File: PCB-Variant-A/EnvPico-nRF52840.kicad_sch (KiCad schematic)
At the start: 49 parts, among them J3 2.54mm header 01x20, J4 2.54mm header 01x20, J5 Conn_01x03_Male, U1 LM3671MF 3.3, U101 nRF52840_holyiot_18010, U2 BQ24072RGT, U3 nRF52840, Y1 32MHz 12pF

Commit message: made a couple of pcb variants for future use maybe
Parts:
- removed U101: nRF52840_holyiot_18010, EnvExtras:nRF52840_holyiot_18010, symbol nrf52840_holyiot_18010:nRF52840_holyiot_18010-kicad-keyboard-parts-ahokore-resc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
- added U4: holyiot-18010, mcu:holyiot-18010, symbol mcu:holyiot-18010
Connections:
- net GND: now also U4.1 (GND), U4.32 (GND), U4.44 (GND)
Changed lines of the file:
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@@
     (pin "2")
   )
-  (symbol (lib_id "nrf52840_holyiot_18010:nRF52840_holyiot_18010-kicad-keyboard-parts-ahokore-rescue") (at 52.07 172.085 0) (unit 1)
+  (symbol (lib_id "mcu:holyiot-18010") (at 44.958 174.752 0) (unit 1)
     (in_bom yes) (on_board yes) (fields_autoplaced)
-    (property "Reference" "U101" (id 0) (at 52.07 132.08 0))
-    (property "Value" "nRF52840_holyiot_18010" (id 1) (at 52.07 134.62 0))
-    (property "Footprint" "EnvExtras:nRF52840_holyiot_18010" (id 2) (at 54.61 161.925 0)
-      (effects (font (size 1.27 1.27)) hide)
-    )
-    (property "Datasheet" "http://www.holyiot.com/tp/2019042516322180424.pdf" (id 3) (at 54.61 161.925 0)
+    (property "Reference" "U4" (id 0) (at 44.958 130.302 0))
+    (property "Value" "holyiot-18010" (id 1) (at 44.958 132.842 0))
+    (property "Footprint" "mcu:holyiot-18010" (id 2) (at 44.958 127.762 0)
+      (effects (font (size 1.27 1.27)) hide)
+    )
+    (property "Datasheet" "" (id 3) (at 83.058 200.152 0)
       (effects (font (size 1.27 1.27)) hide)
     )
@@
     (pin "41")
     (pin "42")
-    (pin "42")
     (pin "43")
+    (pin "44")
     (pin "45")
     (pin "46")
@@
       (reference "U3") (unit 1) (value "nRF52840") (footprint "Package_DFN_QFN:Nordic_AQFN-73-1EP_7x7mm_P0.5mm")
     )
-    (path "/8ee0b195-44f0-4b21-9341-8dba1a90f90e"
-      (reference "U101") (unit 1) (value "nRF52840_holyiot_18010") (footprint "EnvExtras:nRF52840_holyiot_18010")
+    (path "/a4716bf7-5af8-4864-9cee-c215b7ab03ab"
+      (reference "U4") (unit 1) (value "holyiot-18010") (footprint "mcu:holyiot-18010")
     )
     (path "/00000000-0000-0000-0000-00005edb7d8d"

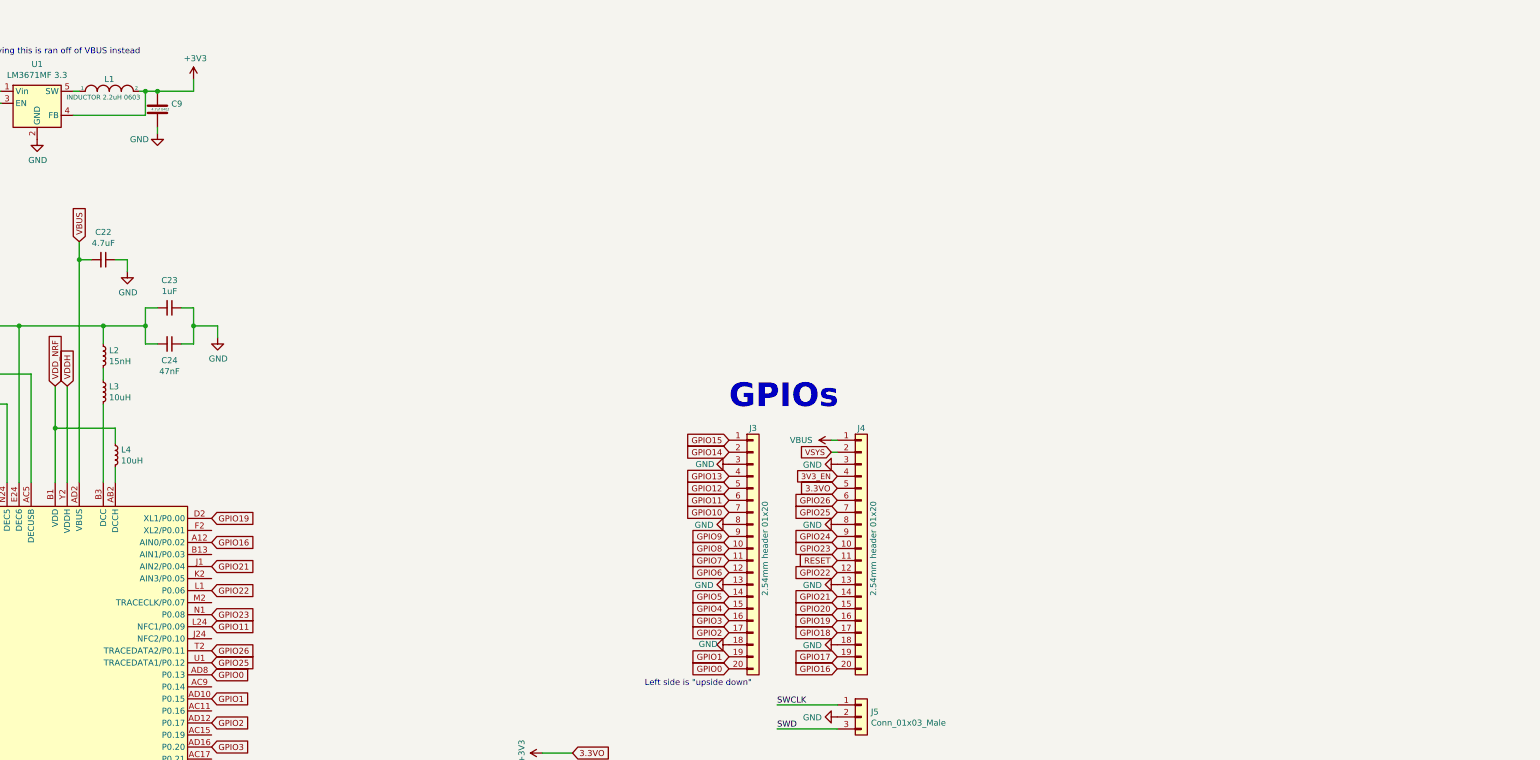
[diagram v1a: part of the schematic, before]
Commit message: added library for QFN version
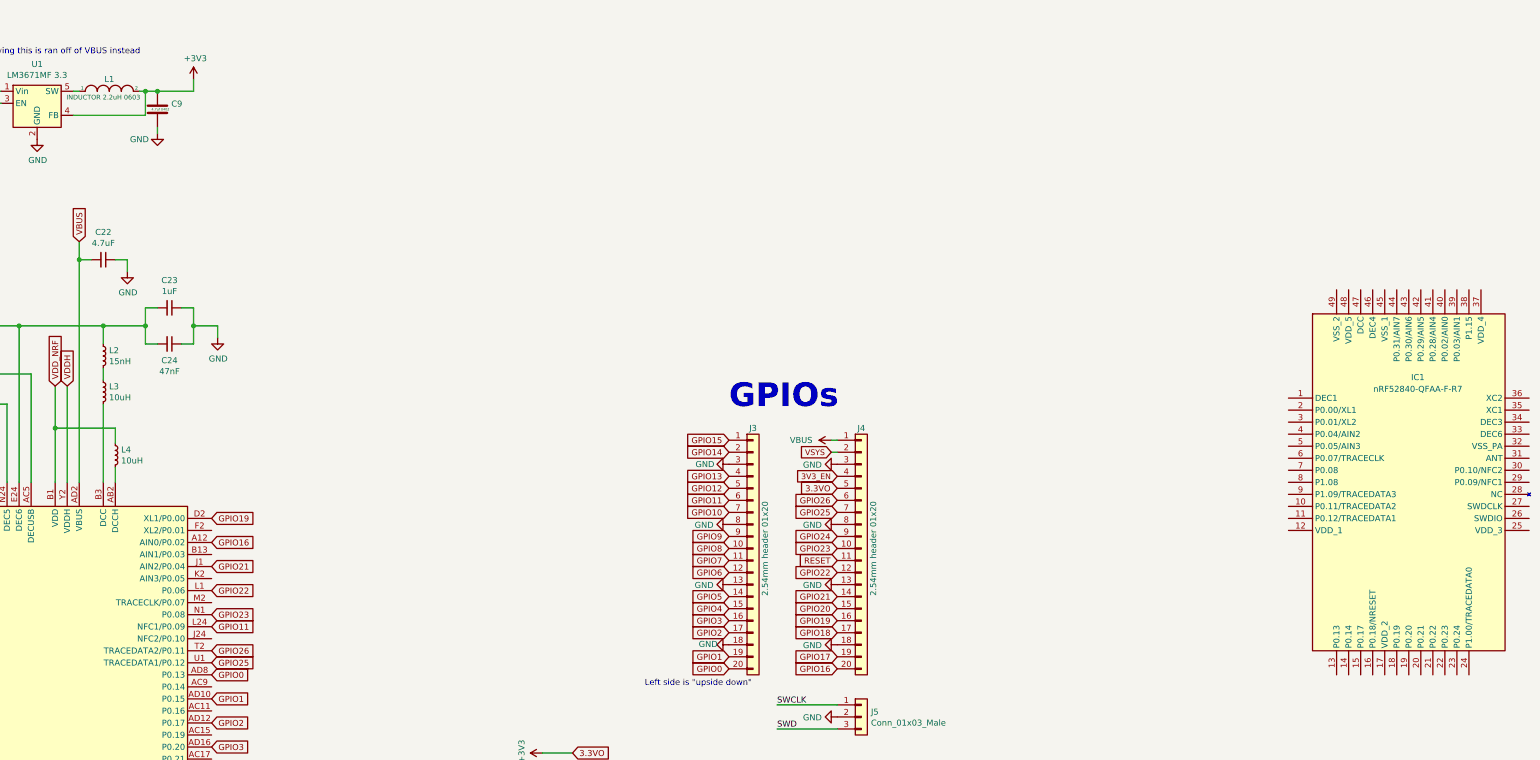
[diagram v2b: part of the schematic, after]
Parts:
- added IC1: nRF52840-QFAA-F-R7, QFN40P600X600X95-49N-D, symbol nRF52840-QFAA-F-R7:nRF52840-QFAA-F-R7

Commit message: started re-design of board.
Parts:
- removed C13: 0402 1pF, Capacitor_SMD:C_0402_1005Metric, symbol Device:C_Small
- removed C8: 0402 1.5pF, Capacitor_SMD:C_0402_1005Metric, symbol Device:C_Small
- removed IC1: nRF52840-QFAA-F-R7, QFN40P600X600X95-49N-D, symbol nRF52840-QFAA-F-R7:nRF52840-QFAA-F-R7
- removed NT1: Net-Tie_2, NetTie:NetTie-2_SMD_Pad0.5mm, symbol Device:Net-Tie_2
- removed R1: 0R 0402, Resistor_SMD:R_0402_1005Metric, symbol Device:R_Small
- removed U4: holyiot-18010, mcu:holyiot-18010, symbol mcu:holyiot-18010
- added L5: 5.6nH 0402, Inductor_SMD:L_0402_1005Metric, symbol Device:L_Small
- AE1: footprint RF_Antenna:Texas_SWRA117D_2.4GHz_Left -> RF_Antenna:Johanson_2450AT43F0100
- C14: value 0402 1pF -> 0402 0.8pF
- C15: value 100nF -> 100nF 0402
- C16: value 100pF -> 100pF 0402
- C17: value 1nF -> 820pF 0402 - DNP
- J5: value Conn_01x03_Male -> BM03B 3P; footprint Connector_PinHeader_2.54mm:PinHeader_1x03_P2.54mm_Vertical -> Connector_JST:JST_SUR_BM03B-SURS-TF_1x03-1MP_P0.80mm_Vertical
- Y1: value 32MHz 12pF -> 32MHz 12pF 2016-4P; footprint Crystal:Crystal_SMD_3225-4Pin_3.2x2.5mm -> Crystal:Crystal_SMD_2016-4Pin_2.0x1.6mm
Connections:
- net VSS_PA is gone; now on net GND: C14.2, U3.F23 (VSS_PA)
- net +3V3: no longer J4.5 (Pin_5)
- net 3V3_EN: no longer J4.4 (Pin_4)
- net GND: no longer J3.13 (Pin_13), J3.18 (Pin_18), J3.3 (Pin_3), J3.8 (Pin_8), J4.13 (Pin_13), J4.18 (Pin_18), J4.3 (Pin_3), J4.8 (Pin_8)
- net GPIO0: no longer J3.20 (Pin_20)
- net GPIO1: no longer J3.19 (Pin_19)
- net GPIO10: no longer J3.7 (Pin_7)
- net GPIO11: no longer J3.6 (Pin_6)
- net GPIO12: no longer J3.5 (Pin_5)
- net GPIO13: no longer J3.4 (Pin_4)
- net GPIO14: no longer J3.2 (Pin_2)
- net GPIO15: no longer J3.1 (Pin_1)
- net GPIO16: no longer J4.20 (Pin_20)
- net GPIO17: no longer J4.19 (Pin_19)
- net GPIO18: no longer J4.17 (Pin_17)
- net GPIO19: no longer J4.16 (Pin_16)
- net GPIO2: no longer J3.17 (Pin_17)
- net GPIO20: no longer J4.15 (Pin_15)
- net GPIO21: no longer J4.14 (Pin_14)
- net GPIO22: no longer J4.12 (Pin_12)
- net GPIO23: no longer J4.10 (Pin_10)
- net GPIO24: no longer J4.9 (Pin_9)
- net GPIO25: no longer J4.7 (Pin_7)
- net GPIO26: no longer J4.6 (Pin_6)
- net GPIO3: no longer J3.16 (Pin_16)
- net GPIO4: no longer J3.15 (Pin_15)
- net GPIO5: no longer J3.14 (Pin_14)
- net GPIO6: no longer J3.12 (Pin_12)
- net GPIO7: no longer J3.11 (Pin_11)
- net GPIO8: no longer J3.10 (Pin_10)
- net GPIO9: no longer J3.9 (Pin_9)
- net RESET: no longer J4.11 (Pin_11)
- net VBUS: no longer J4.1 (Pin_1)
- net VSYS: no longer J4.2 (Pin_2)
- net at C14.1, U3.H23 (ANT): now also L5.2
- net at AE1.1 (A): now also L5.1
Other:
- note added: "Antenna Trace needs to be 0.6322mm for 0.15mm zone clearance"
- note added: "trace should be 50 ohms to antenna"
- note removed: "(Zero Ohms)"
- note removed: "i forgot what this was for. i think it was for a decoupling cap."
- moved on the sheet: J3, J4
